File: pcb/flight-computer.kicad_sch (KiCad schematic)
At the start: 12 parts, among them SW1 PTS815, U1 STM32F446RETx

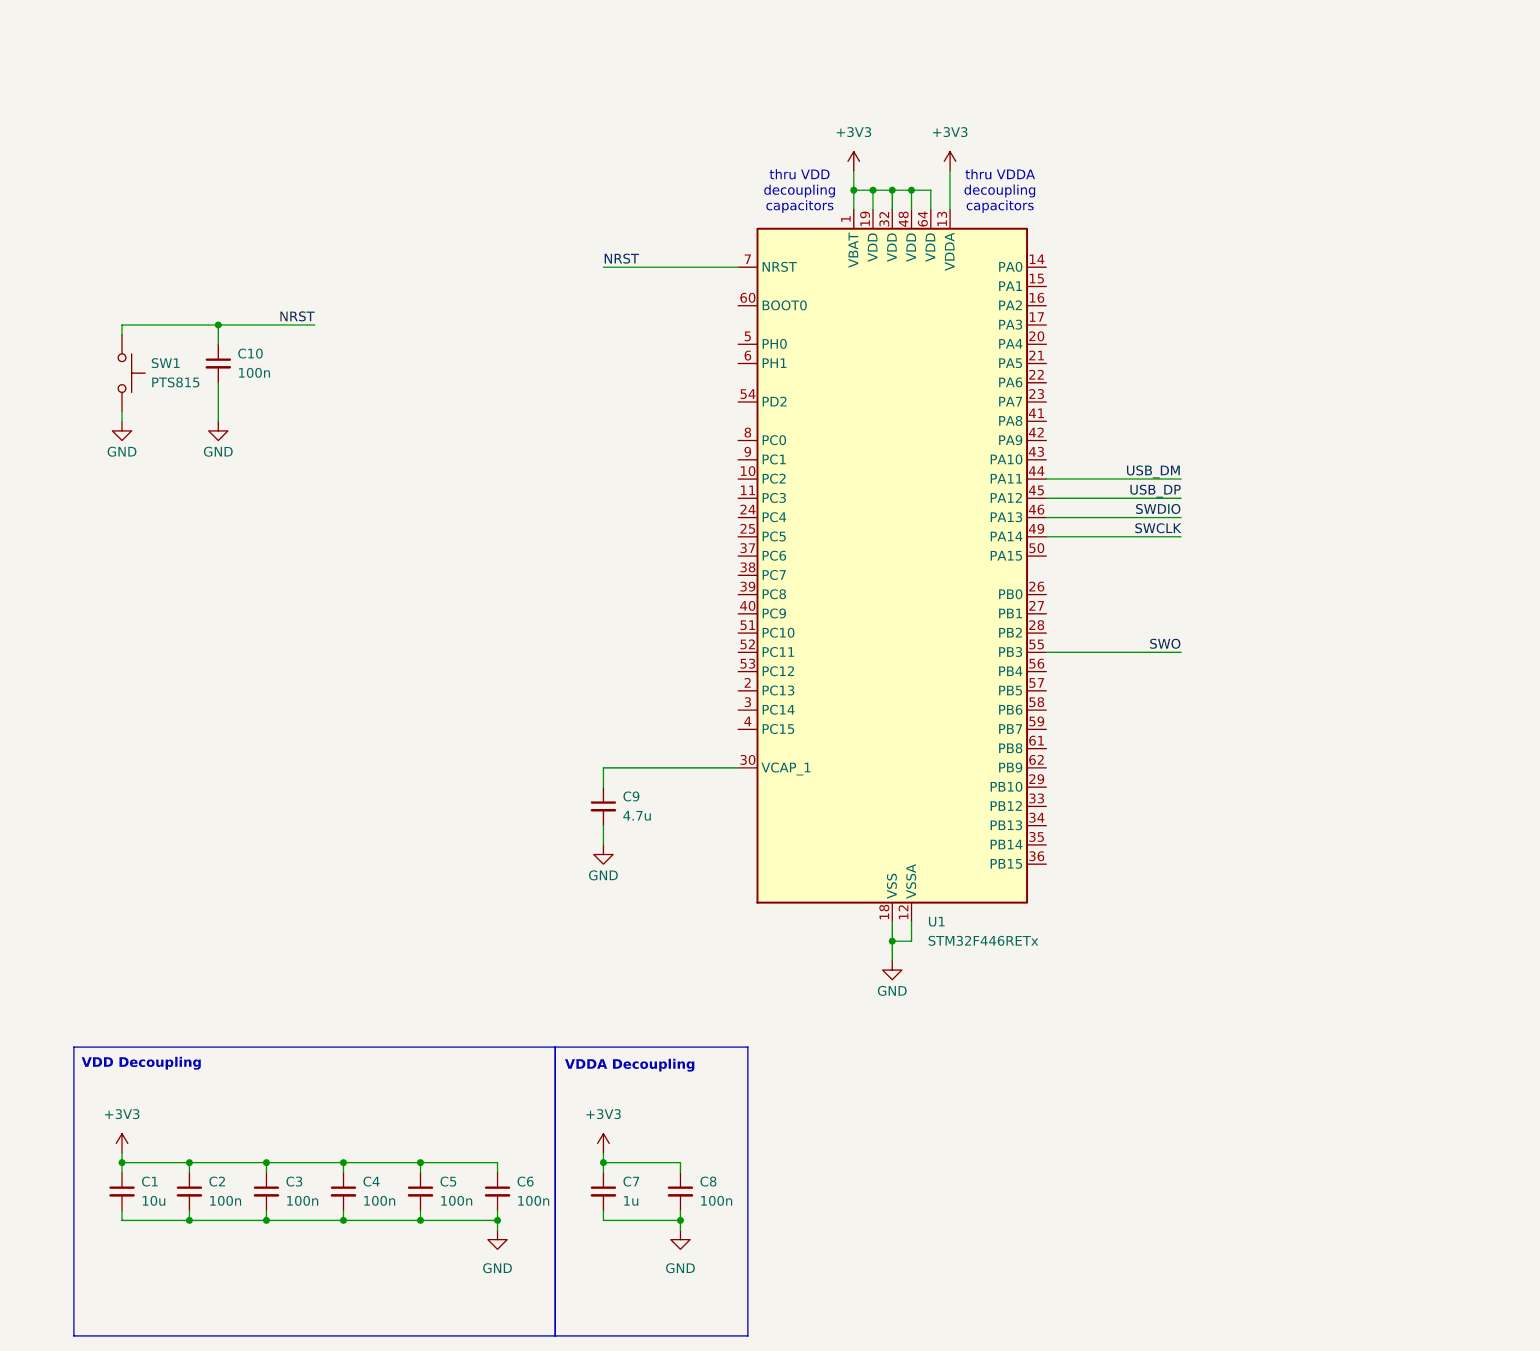
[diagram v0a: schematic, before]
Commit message: Finished GPIO assignment
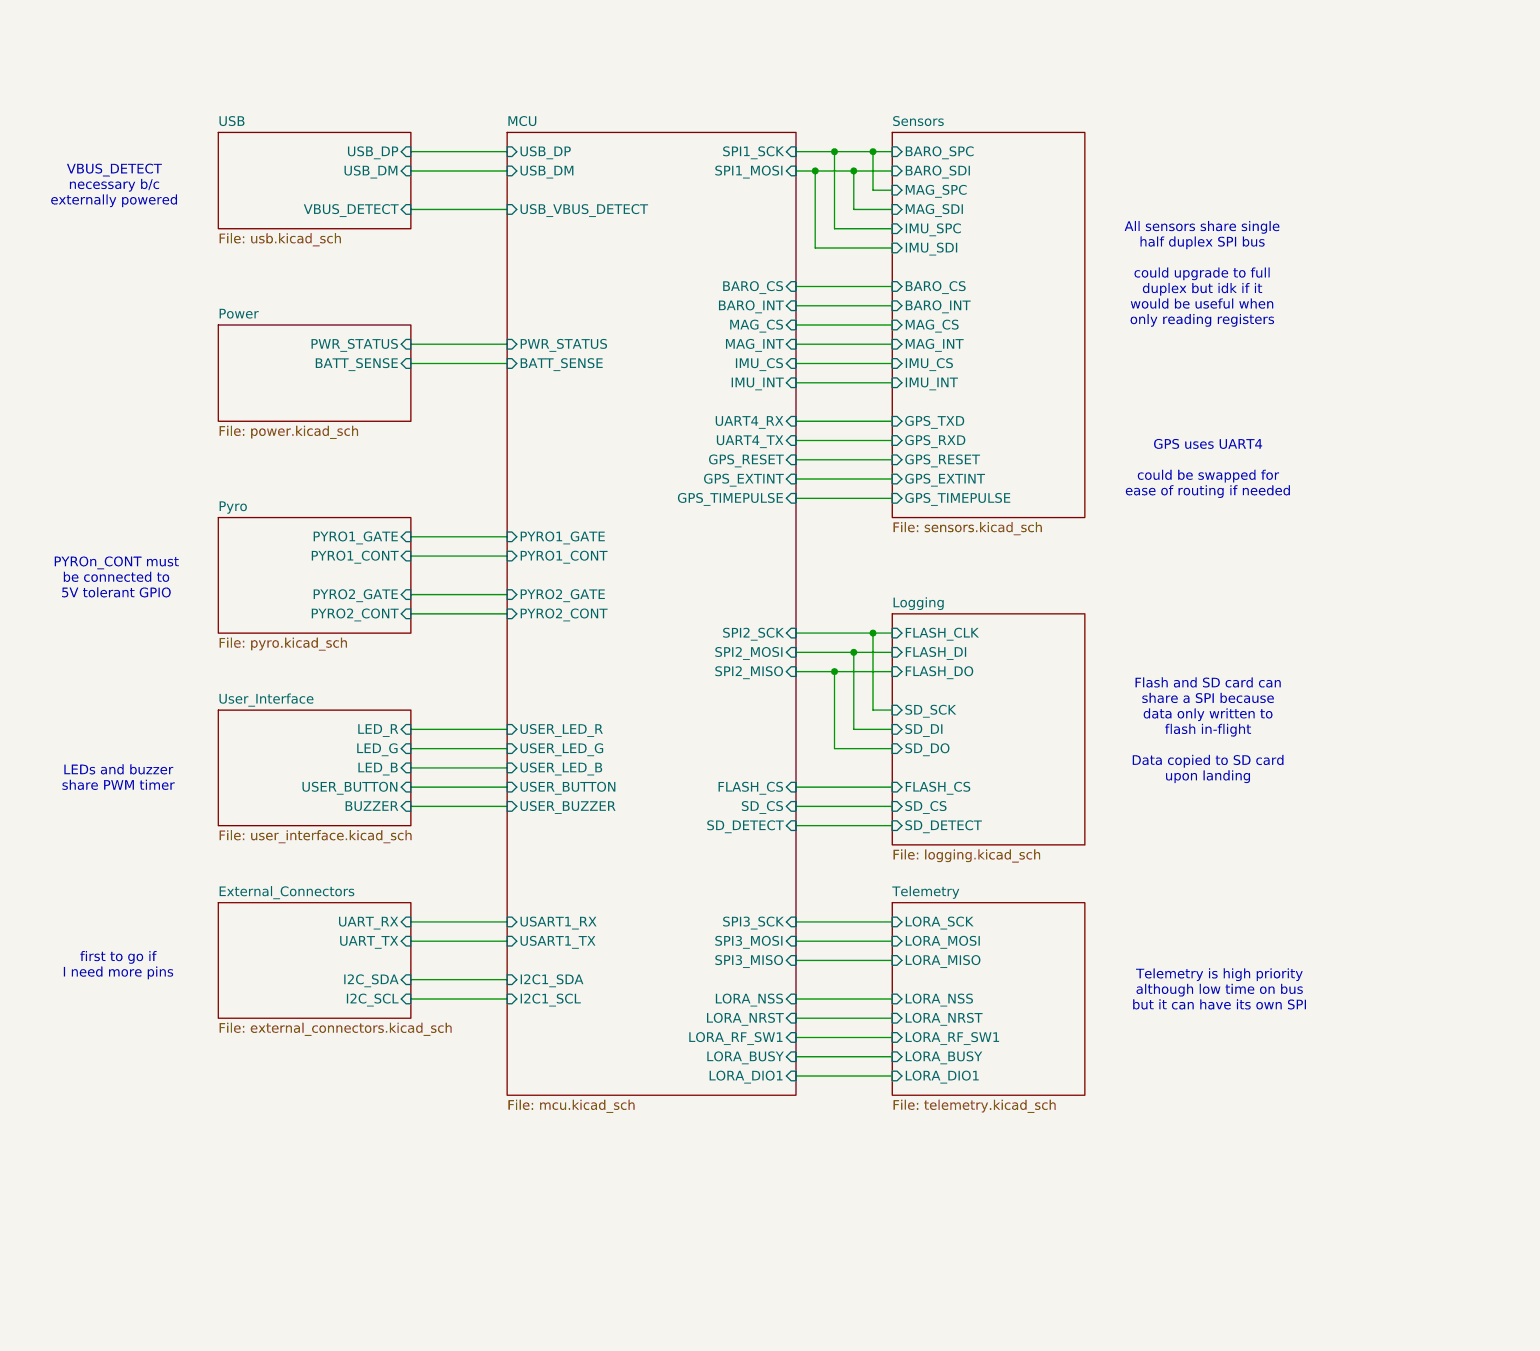
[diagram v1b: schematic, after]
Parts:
- removed C1: 10u, symbol Device:C_Small
- removed C10, C2, C3, C4, C5, C6, C8: 100n, symbol Device:C_Small
- removed C7: 1u, symbol Device:C_Small
- removed C9: 4.7u, symbol Device:C_Small
- removed SW1: PTS815, symbol Switch:SW_Push
- removed U1: STM32F446RETx, Package_QFP:LQFP-64_10x10mm_P0.5mm, symbol MCU_ST_STM32F4:STM32F446RETx
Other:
- added sheet External_Connectors (external_connectors.kicad_sch)
- added sheet Logging (logging.kicad_sch)
- added sheet MCU (mcu.kicad_sch)
- added sheet Power (power.kicad_sch)
- added sheet Pyro (pyro.kicad_sch)
- added sheet Sensors (sensors.kicad_sch)
- added sheet Telemetry (telemetry.kicad_sch)
- added sheet USB (usb.kicad_sch)
- added sheet User_Interface (user_interface.kicad_sch)
- note added: "All sensors share single half duplex SPI bus could upgrade to full duplex but idk if it would be useful when only reading registers"
- note added: "Flash and SD card can share a SPI because data only written to flash in-flight Data copied to SD card upon landing"
- note added: "GPS uses UART4 could be swapped for ease of routing if needed"
- note added: "LEDs and buzzer share PWM timer"
- note added: "PYROn_CONT must be connected to 5V tolerant GPIO"
- note added: "Telemetry is high priority although low time on bus but it can have its own SPI"
- note added: "VBUS_DETECT necessary b/c externally powered"
- note added: "first to go if I need more pins"
- note removed: "VDD Decoupling"
- note removed: "VDDA Decoupling"
- note removed: "thru VDD decoupling capacitors"
- note removed: "thru VDDA decoupling capacitors"

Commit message: Improve inter sheet connections
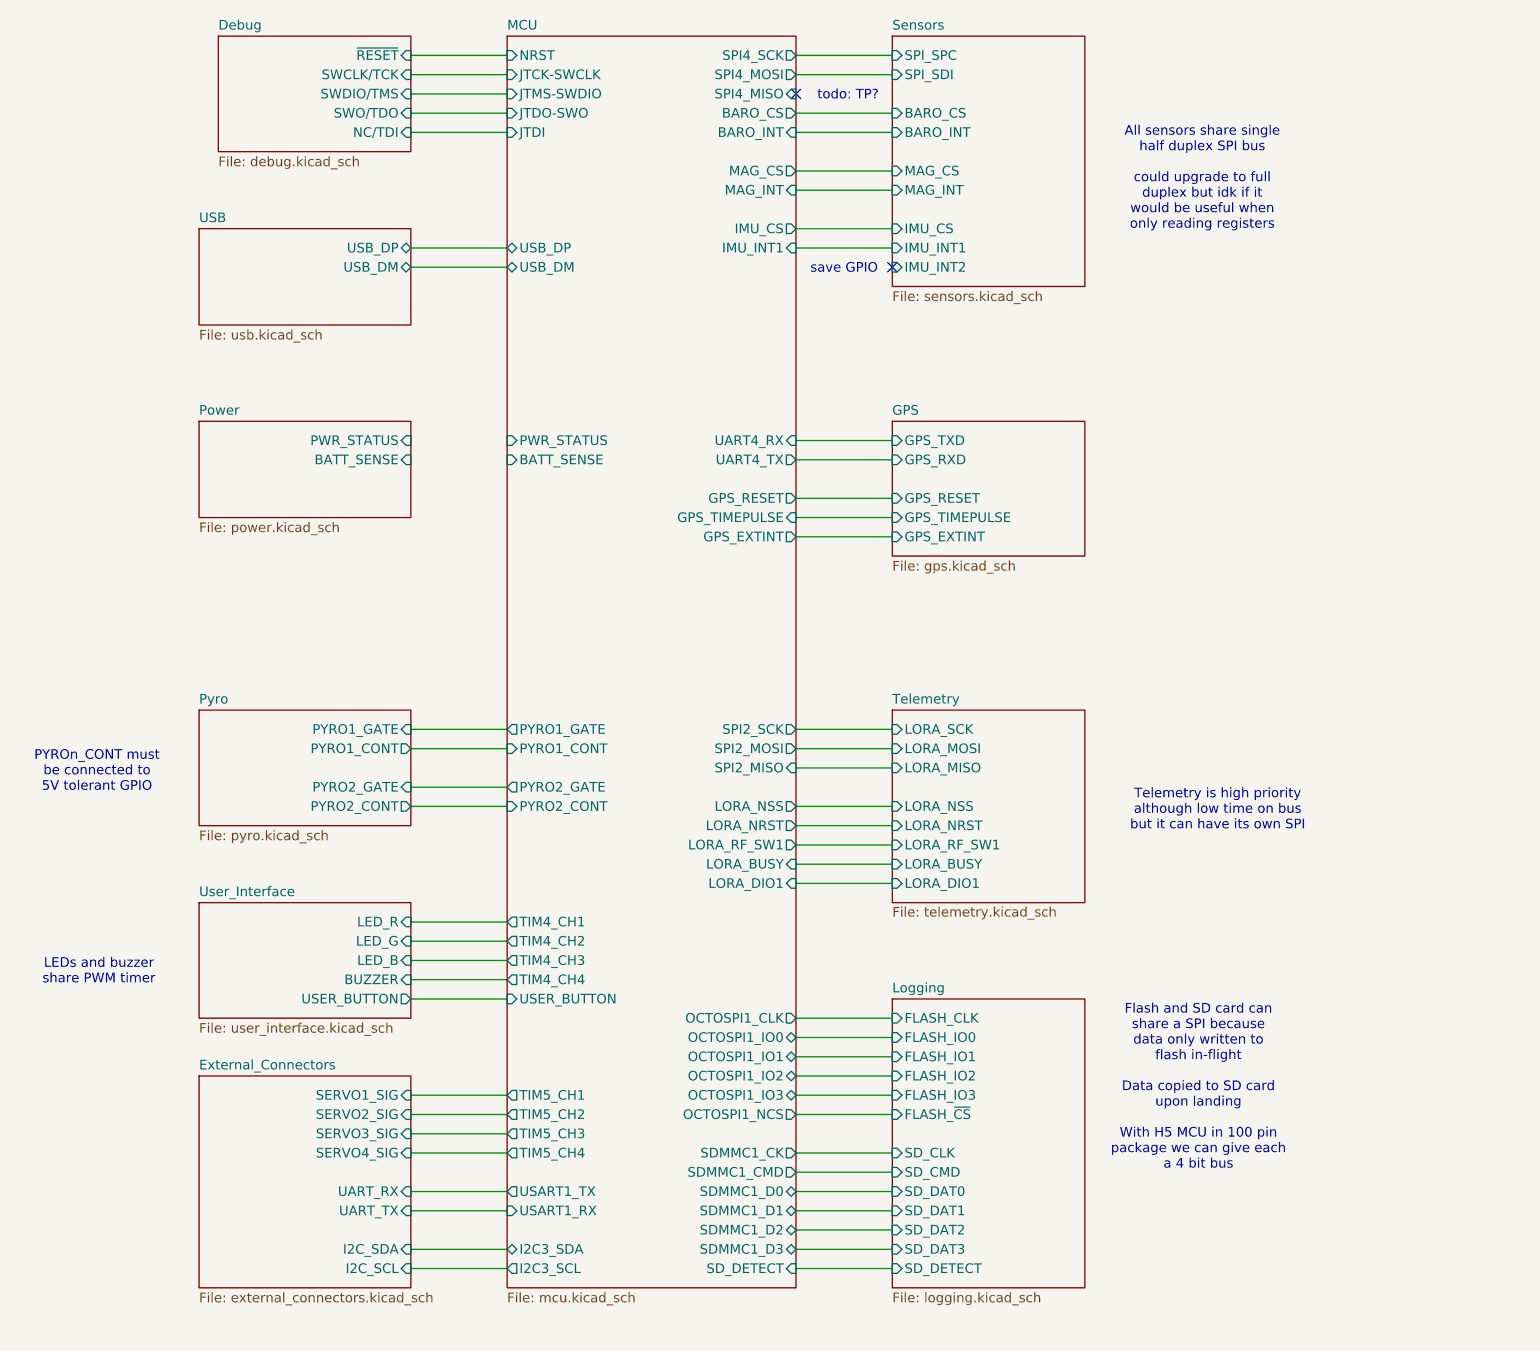
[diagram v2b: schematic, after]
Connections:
- no-connect marks 0 -> 2
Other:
- added sheet Debug (debug.kicad_sch)
- added sheet GPS (gps.kicad_sch)
- sheet External_Connectors ports: added SERVO1_SIG, SERVO2_SIG, SERVO3_SIG, SERVO4_SIG; removed none
- sheet Logging ports: added FLASH_IO0, FLASH_IO1, FLASH_IO2, FLASH_IO3, FLASH_~{CS}, SD_CLK, SD_CMD, SD_DAT0, SD_DAT1, SD_DAT2, SD_DAT3; removed FLASH_CS, FLASH_DI, FLASH_DO, SD_CS, SD_DI, SD_DO, SD_SCK
- sheet MCU ports: added I2C3_SCL, I2C3_SDA, IMU_INT1, JTCK-SWCLK, JTDI, JTDO-SWO, JTMS-SWDIO, NRST, OCTOSPI1_CLK, OCTOSPI1_IO0, OCTOSPI1_IO1, OCTOSPI1_IO2, OCTOSPI1_IO3, OCTOSPI1_NCS, SDMMC1_CK, SDMMC1_CMD, SDMMC1_D0, SDMMC1_D1, SDMMC1_D2, SDMMC1_D3, SPI4_MISO, SPI4_MOSI, SPI4_SCK, TIM4_CH1, TIM4_CH2, TIM4_CH3, TIM4_CH4, TIM5_CH1, TIM5_CH2, TIM5_CH3, TIM5_CH4; removed FLASH_CS, I2C1_SCL, I2C1_SDA, IMU_INT, SD_CS, SPI1_MOSI, SPI1_SCK, SPI3_MISO, SPI3_MOSI, SPI3_SCK, USB_VBUS_DETECT, USER_BUZZER, USER_LED_B, USER_LED_G, USER_LED_R
- sheet Sensors ports: added IMU_INT1, IMU_INT2, SPI_SDI, SPI_SPC; removed BARO_SDI, BARO_SPC, GPS_EXTINT, GPS_RESET, GPS_RXD, GPS_TIMEPULSE, GPS_TXD, IMU_INT, IMU_SDI, IMU_SPC, MAG_SDI, MAG_SPC
- sheet USB ports: added none; removed VBUS_DETECT
- note added: "Flash and SD card can share a SPI because data only written to flash in-flight Data copied to SD card upon landing With H5 MCU in 100 pin package we can give each a 4 bit bus"
- note added: "save GPIO"
- note added: "todo: TP?"
- note removed: "Flash and SD card can share a SPI because data only written to flash in-flight Data copied to SD card upon landing"
- note removed: "GPS uses UART4 could be swapped for ease of routing if needed"
- note removed: "VBUS_DETECT necessary b/c externally powered"
- note removed: "first to go if I need more pins"
- title: (none) -> Flight Computer

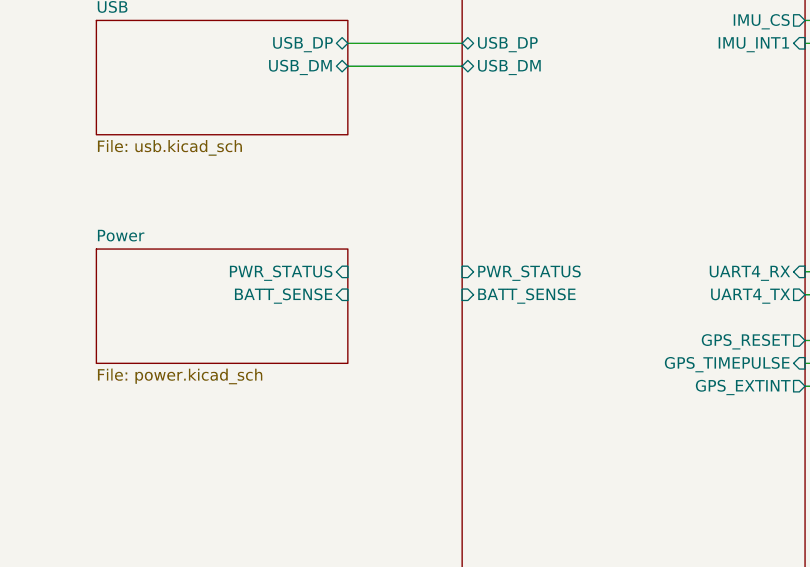
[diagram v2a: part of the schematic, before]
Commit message: Shuffle pins to allow for additional I2C
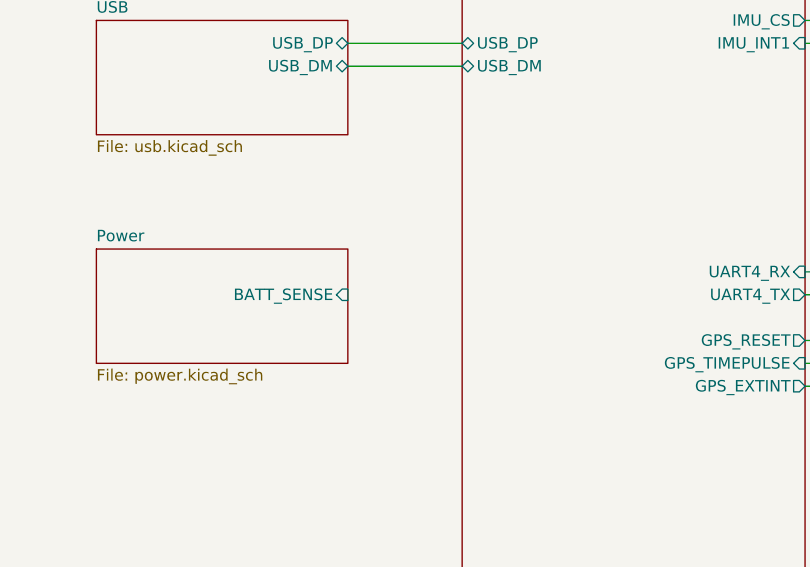
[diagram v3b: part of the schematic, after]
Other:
- sheet MCU ports: added none; removed BATT_SENSE, PWR_STATUS
- sheet Power ports: added none; removed PWR_STATUS
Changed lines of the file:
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@@
-			)
-		)
-		(pin "PWR_STATUS" input
-			(at 63.5 78.74 0)
-			(effects
-				(font
-					(size 1.27 1.27)
-				)
-				(justify right)
 			)
 		)
@@
 			)
 		)
-		(pin "BATT_SENSE" input
-			(at 76.2 81.28 180)
-			(effects
-				(font
-					(size 1.27 1.27)
-				)
-				(justify left)
-			)
-		)
 		(pin "GPS_RESET" output
 			(at 114.3 86.36 0)
@@
 			(effects
 				(font
-					(size 1.27 1.27)
-				)
-				(justify left)
-			)
-		)
-		(pin "PWR_STATUS" input
-			(at 76.2 78.74 180)
-			(effects
-				(font
